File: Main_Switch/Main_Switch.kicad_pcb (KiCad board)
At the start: 4 copper layers, 44.4 x 41.4 mm, 45 parts, among them J1 BAT+, J2 Load+, J3 Coil, J4 Switch, J5 GND, J6 TC2030, Q1 XR20P10F, Q2 XR20P10F, Q3 2N7002, Q4 AO3400A, U1 CH32V003FxUx, U2 L78L05_SOT89, U4 LMR51610XDBVR

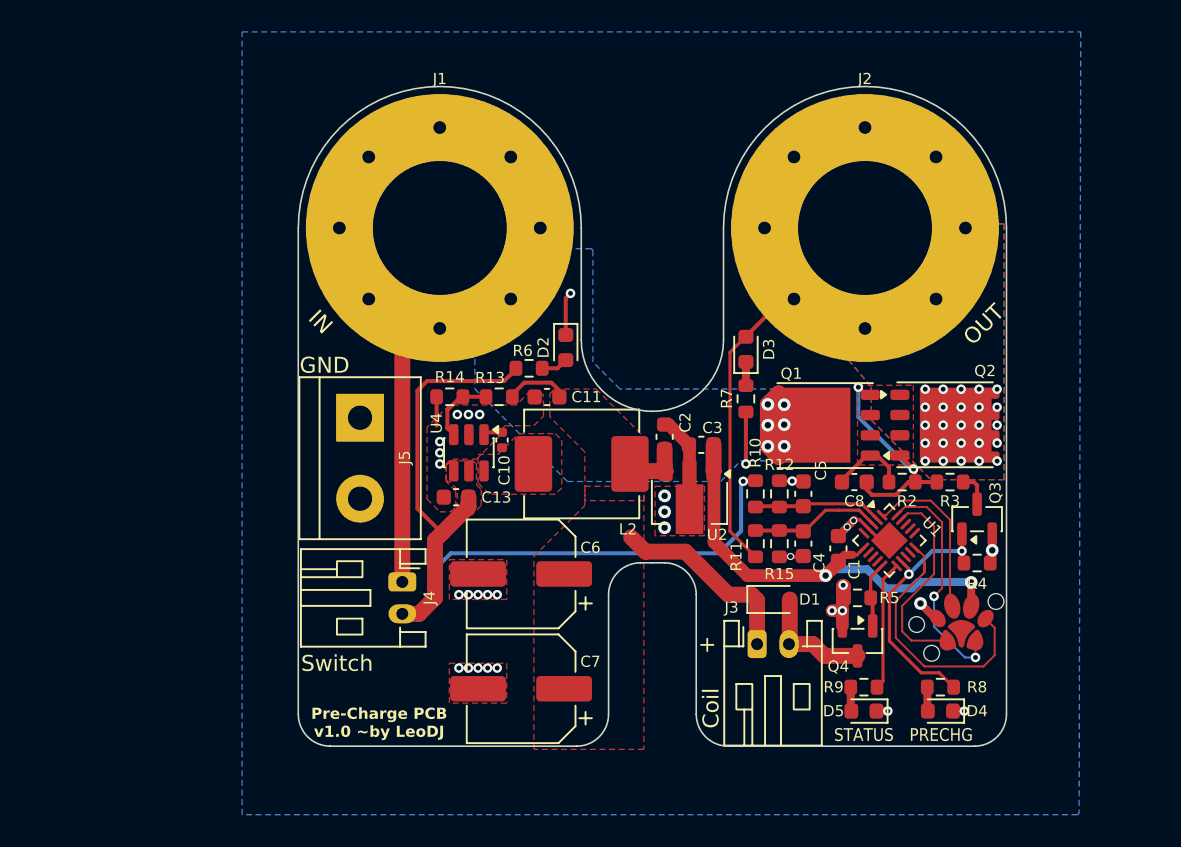
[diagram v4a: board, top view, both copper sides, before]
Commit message: modify PCB for GV200 and beefen up 12V DCDC
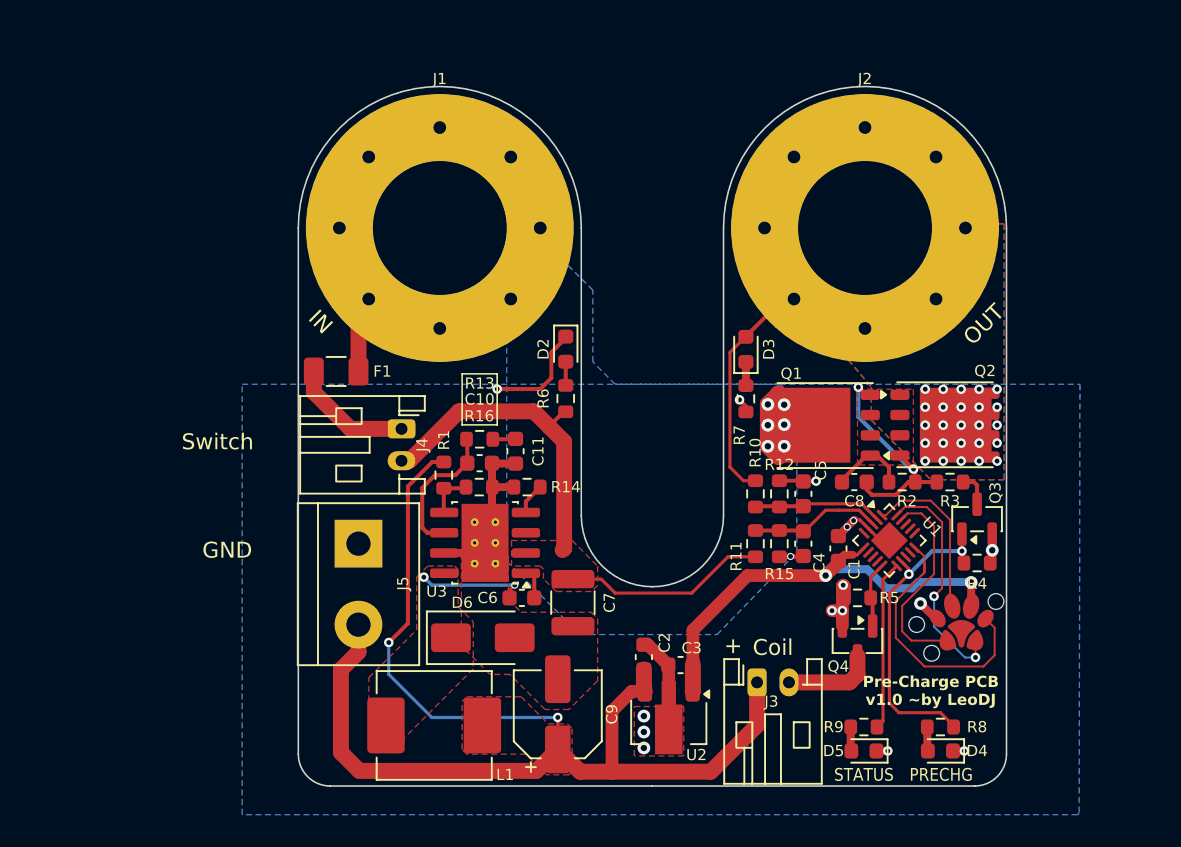
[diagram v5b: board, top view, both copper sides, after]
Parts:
- removed C13: 1u 100V, Capacitor_SMD:C_0603_1608Metric
- removed D1: B110WS, Diode_SMD:D_SOD-323
- removed L2: 68uH, Inductor_SMD:L_Sunlord_MWSA0605S
- removed U4: LMR51610XDBVR, Package_TO_SOT_SMD:SOT-23-6
- added C9: 47u Polymer, Capacitor_SMD:CP_Elec_5x5.8, F.Cu at (142.3, 124.9)
- added D6: SS56F, Diode_SMD:D_SMA, F.Cu at (137.6, 120.1)
- added F1: 1A, Fuse:Fuse_1206_3216Metric, F.Cu at (128.4, 103.4)
- added L1: 10uH, Inductor_SMD:L_Sunlord_MWSA0605S, F.Cu at (134.5, 125.6)
- added R1: 150k, Resistor_SMD:R_0603_1608Metric, F.Cu at (135.1, 109.9)
- added R16: 11k, Resistor_SMD:R_0603_1608Metric, F.Cu at (137.3, 110.6)
- added U3: TPS54560BDDA, Package_SO:Texas_R-PDSO-G8_EP2.95x4.9mm_Mask2.4x3.1mm_ThermalVias, F.Cu at (137.7, 114.1)
- C10: value 100n -> 6p8; footprint Capacitor_SMD:C_0402_1005Metric -> Capacitor_SMD:C_0603_1608Metric
- C11: value 22u 16V -> 1n
- C6: value 470u 16V -> 100n; footprint Capacitor_SMD:CP_Elec_6.3x7.7 -> Capacitor_SMD:C_0603_1608Metric
- C7: value 470u 16V -> 10u 100V; footprint Capacitor_SMD:CP_Elec_6.3x7.7 -> Capacitor_SMD:C_1210_3225Metric
- Q4: value AO3400A -> SSM3K341R
- R10, R11, R6, R7: value 100k -> 120k
- R13: value 150k -> 47k
- R14: value 11k -> 120k
- moved C3 13.9 mm to (150.0, 121.8)
- moved C2 13.9 mm to (147.7, 121.3)
- moved U2 13.9 mm to (149.2, 125.4)
- moved J4 9.60 mm to (132.5, 107.0)
- moved J5 7.90 mm to (129.8, 114.2)
- moved R14 7.46 mm to (140.3, 110.6)
- moved C7 6.30 mm to (143.2, 117.9), turned to -90 degrees
- moved C11 3.93 mm to (139.6, 108.4), turned to -90 degrees
- moved R6 2.98 mm to (142.8, 105.1), turned to 90 degrees
- moved R13 2.93 mm to (137.4, 107.6), turned to 0 degrees
- moved G*** 2.74 mm to (137.3, 122.3)
- moved D4 2.50 mm to (166.3, 127.2)
- moved D5 2.50 mm to (161.5, 127.2)
- moved R8 2.50 mm to (166.3, 125.7)
- moved R9 2.50 mm to (161.5, 125.7)
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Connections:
- C10 pad 1: Net-(U4-SW) -> Net-(U3-COMP)
- C10 pad 2: Net-(U4-CB) -> GND
- C11 pad 1: +12V -> Net-(C11-Pad1)
- C4 pad 1: SNS_VIN -> SNS_VOUT
- C5 pad 1: SNS_VOUT -> SNS_VIN
- C6 pad 1: +12V -> Net-(U3-BOOT)
- C6 pad 2: GND -> /SW
- C7 pad 1: +12V -> BUCK_VIN
- J4 pad 1: BAT+ -> Net-(J4-Pin_1)
- J5 pad 2: GND -> +12V
- R10 pad 1: BUCK_VIN -> OUT+
- R10 pad 2: SNS_VIN -> SNS_VOUT
- R11 pad 1: OUT+ -> BUCK_VIN
- R11 pad 2: SNS_VOUT -> SNS_VIN
- R12 pad 1: SNS_VIN -> SNS_VOUT
- R13 pad 1: +12V -> Net-(U3-COMP)
- R13 pad 2: Net-(U4-FB) -> Net-(C11-Pad1)
- R14 pad 1: Net-(U4-FB) -> Net-(U3-RT/CLK)
- R15 pad 1: SNS_VOUT -> SNS_VIN
- U1 pad 2: SNS_VIN -> SNS_VOUT
- U1 pad 3: SNS_VOUT -> SNS_VIN
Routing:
- net +12V: track 22.9 -> 76.8 mm, vias 0 -> 2
- net BUCK_VIN: track 54.4 -> 33.3 mm, vias 1 -> 0
- net BAT+: track 31.7 -> 19.7 mm
- net GND: track 29.7 -> 41.2 mm, vias 32 -> 16
- net Net-(U3-COMP): track 0.00 -> 8.99 mm
- net Net-(J4-Pin_1): track 0.00 -> 7.75 mm
- net /SW: track 0.00 -> 6.84 mm, vias 0 -> 2
- net Net-(U4-FB): track 4.48 -> 0.00 mm
- net OUT+: track 25.2 -> 20.9 mm
- net PRECHARGE: track 16.7 -> 20.1 mm
- net Net-(U3-FB): track 0.00 -> 2.96 mm
- net LED: track 8.12 -> 10.6 mm
- net Net-(U3-BOOT): track 0.00 -> 2.05 mm
- net Net-(U3-RT/CLK): track 0.00 -> 1.97 mm
- net Net-(J3-Pin_2): track 7.43 -> 5.67 mm
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- added copper zone on F.Cu, net /SW
- removed copper zone on F.Cu, net Net-(U4-SW)
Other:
- board size 44.4 x 41.4 mm -> 44.4 x 43.9 mm

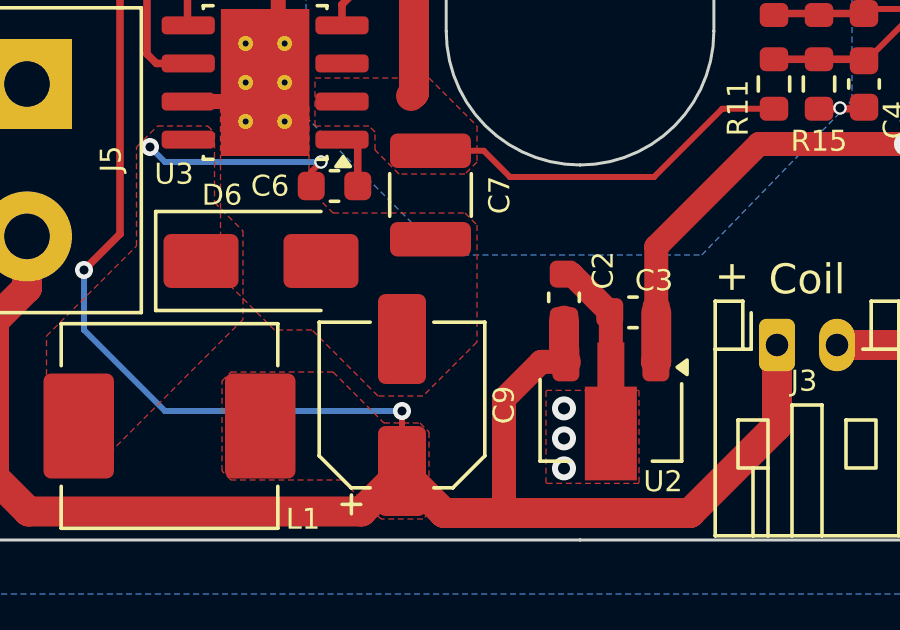
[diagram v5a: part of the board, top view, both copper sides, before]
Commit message: [Switch] last fixes and generate gerbers
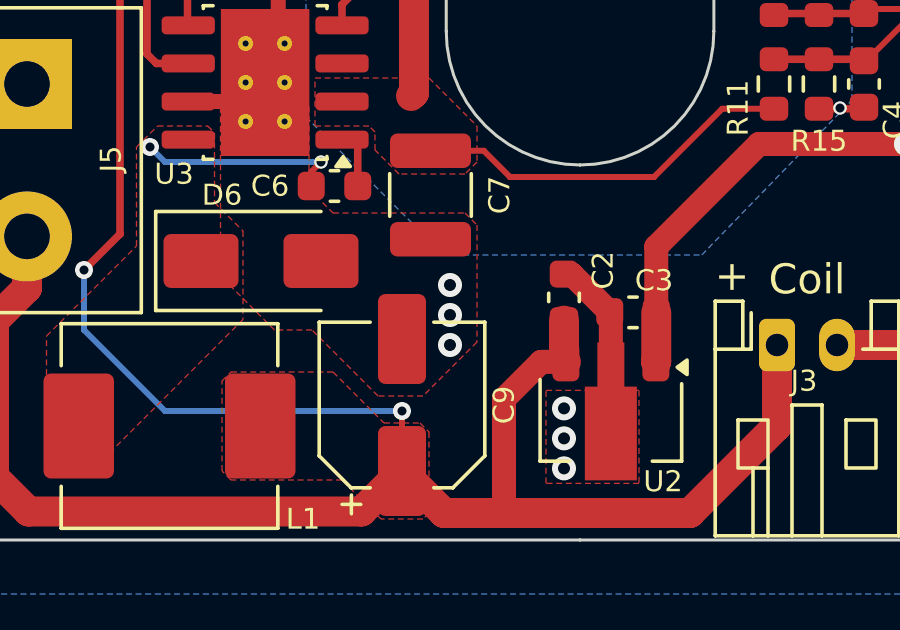
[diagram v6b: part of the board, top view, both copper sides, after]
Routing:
- net GND: vias 16 -> 19

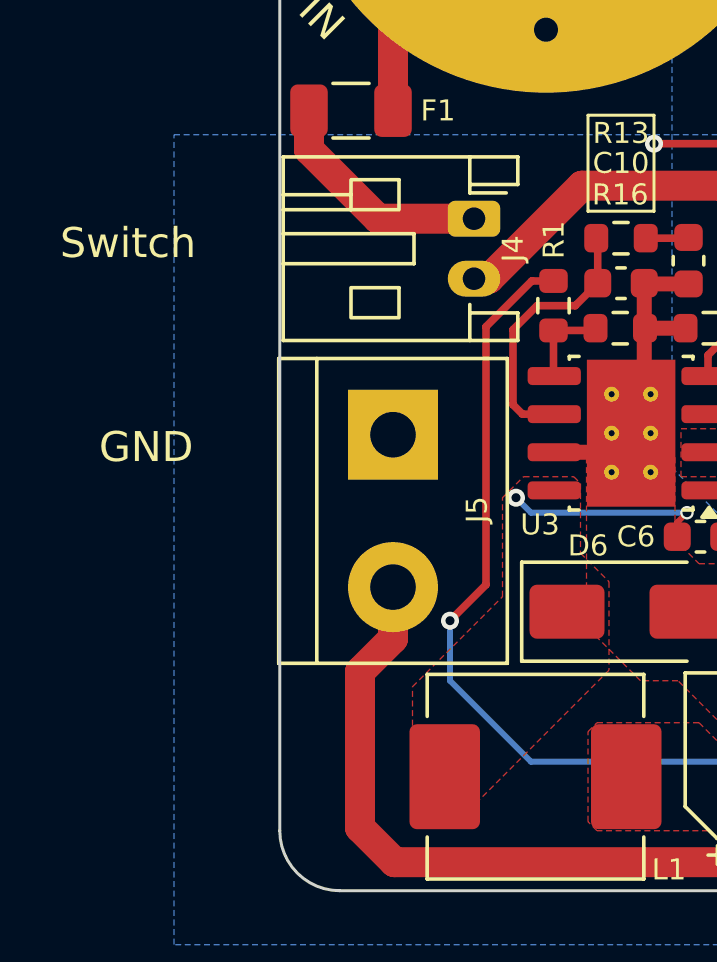
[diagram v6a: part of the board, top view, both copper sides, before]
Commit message: [Switch] Minor silkscreen tweaks and bump to 6L for cheaper JLCPCB order
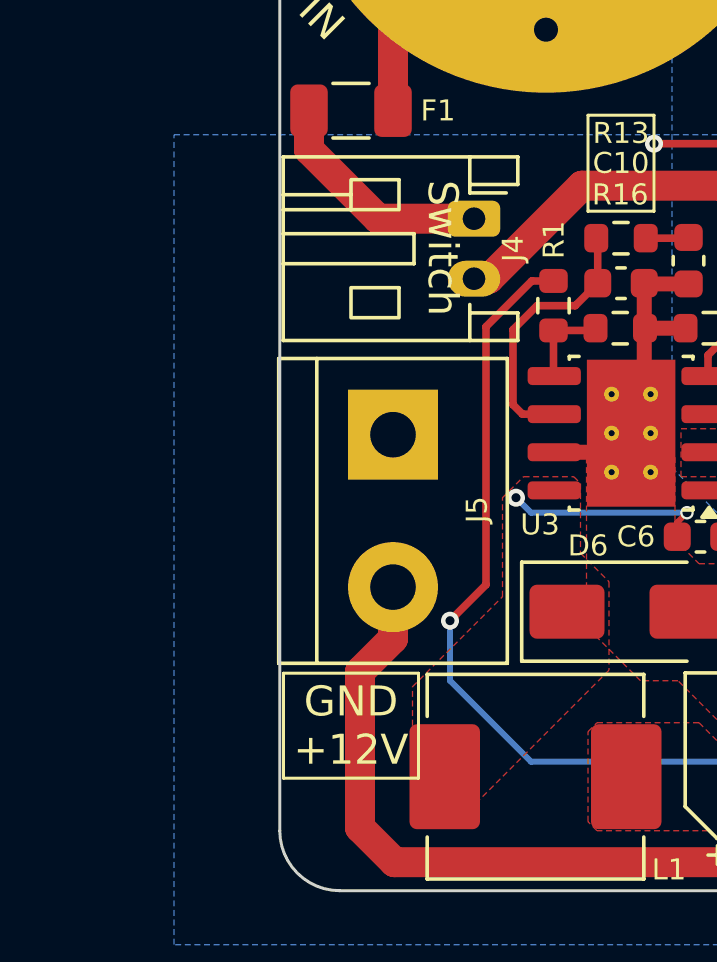
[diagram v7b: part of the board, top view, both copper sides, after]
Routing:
- added copper zone on In3.Cu, net GND
- added copper zone on In4.Cu, net GND
- added copper zone on In3.Cu, net OUT+
- added copper zone on In4.Cu, net OUT+
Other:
- copper layers 4 -> 6
- board text added: "+12V"
- board text added: "GND +12V"
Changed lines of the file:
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@@
 		(4 "In1.Cu" signal)
 		(6 "In2.Cu" signal)
+		(8 "In3.Cu" signal)
+		(10 "In4.Cu" signal)
 		(2 "B.Cu" signal)
 		(9 "F.Adhes" user "F.Adhesive")
@@
 			(layer "dielectric 2"
 				(type "core")
-				(thickness 1.24)
+				(thickness 0.535)
 				(material "FR4")
 				(epsilon_r 4.5)
@@
 				(loss_tangent 0.02)
 			)
+			(layer "In3.Cu"
+				(type "copper")
+				(thickness 0.035)
+			)
+			(layer "dielectric 4"
+				(type "core")
+				(thickness 0.535)
+				(material "FR4")
+				(epsilon_r 4.5)
+				(loss_tangent 0.02)
+			)
+			(layer "In4.Cu"
+				(type "copper")
+				(thickness 0.035)
+			)
+			(layer "dielectric 5"
+				(type "prepreg")
+				(thickness 0.1)
+				(material "FR4")
+				(epsilon_r 4.5)
+				(loss_tangent 0.02)
+			)
 			(layer "B.Cu"
 				(type "copper")
@@
 		(capping no)
 		(filling no)
+		(zone_defaults)
 		(aux_axis_origin 134.874 94.374)
 		(grid_origin 134.874 94.374)
@@
 	)
 	(gr_rect
+		(start 126.124 122.124)
+		(end 130.624 125.624)
+		(stroke
+			(width 0.1)
+			(type default)
+		)
+		(fill no)
+		(layer "F.SilkS")
+	)
+	(gr_rect
 		(start 136.274 103.524)
 		(end 138.474 106.724)
@@
 		)
 	)
-	(gr_text "Switch"
-		(at 118.674 108.374 0)
+	(gr_text "GND\n+12V"
+		(at 128.374 123.874 0)
 		(layer "F.SilkS")
 		(effects
@@
 				(thickness 0.15)
 			)
-			(justify left bottom)
 		)
 	)
-	(gr_text "GND"
-		(at 119.974 115.174 0)
+	(gr_text "+"
+		(at 153.274 120.574 0)
 		(layer "F.SilkS")
 		(effects
@@
 				(thickness 0.15)
 			)
-			(justify left bottom)
 		)
 	)
-	(gr_text "+"
-		(at 153.274 120.574 0)
+	(gr_text "Coil"
+		(at 155.774 121.274 0)
 		(layer "F.SilkS")
 		(effects
@@
 				(thickness 0.15)
 			)
+			(justify bottom)
 		)
 	)
-	(gr_text "Coil"
-		(at 155.774 121.274 0)
+	(gr_text "OUT\n"
+		(at 168.374 101.874 45)
 		(layer "F.SilkS")
 		(effects
@@
 				(thickness 0.15)
 			)
-			(justify bottom)
+			(justify left bottom)
 		)
 	)
-	(gr_text "OUT\n"
-		(at 168.374 101.874 45)
+	(gr_text "Switch"
+		(at 130.844 105.684 270)
 		(layer "F.SilkS")
 		(effects
@@
 		)
 	)
+	(gr_text "Switch"
+		(at 127.874 110.374 -90)
+		(layer "B.SilkS")
+		(effects
+			(font
+				(size 1 1)
+				(thickness 0.15)
+			)
+			(justify left bottom mirror)
+		)
+	)
 	(gr_text "https://github.com/\nRainbowLabsDE/Torquee"
 		(at 159.274 127.774 0)
@@
 	)
 	(gr_text "+"
+		(at 130.124 106.374 180)
+		(layer "B.SilkS")
+		(effects
+			(font
+				(size 1 1)
+				(thickness 0.15)
+			)
+			(justify left bottom mirror)
+		)
+	)
+	(gr_text "+"
 		(at 152.574 122.274 180)
 		(layer "B.SilkS")
@@
 		)
 	)
+	(gr_text "+12V"
+		(at 126.874 119.374 270)
+		(layer "B.SilkS")
+		(effects
+			(font
+				(size 1 1)
+				(thickness 0.15)
+			)
+			(justify mirror)
+		)
+	)
+	(gr_text "GND"
+		(at 126.88447 114.1827 270)
+		(layer "B.SilkS")
+		(effects
+			(font
+				(size 1 1)
+				(thickness 0.15)
+			)
+			(justify mirror)
+		)
+	)
 	(segment
 		(start 140.729 116.029)
@@
 	(zone
 		(net "OUT+")
-		(layers "F.Cu" "B.Cu" "In1.Cu" "In2.Cu")
+		(layers "F.Cu" "B.Cu" "In1.Cu" "In2.Cu" "In3.Cu" "In4.Cu")
 		(hatch edge 0.5)
 		(priority 2)
@@
 	(zone
 		(net "GND")
-		(layers "B.Cu" "In1.Cu" "In2.Cu")
+		(layers "B.Cu" "In1.Cu" "In2.Cu" "In3.Cu" "In4.Cu")
 		(hatch edge 0.5)
 		(connect_pads yes
